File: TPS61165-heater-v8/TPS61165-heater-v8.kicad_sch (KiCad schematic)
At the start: 33 parts, among them J1 USB_C_KoreanHroparts_6P, J2 A2001WR-2P, J3 A2001WR-2P, J5 A2001WR-2P, U1 TPS61165, U2 KAQY212A, U3 INA219AxD

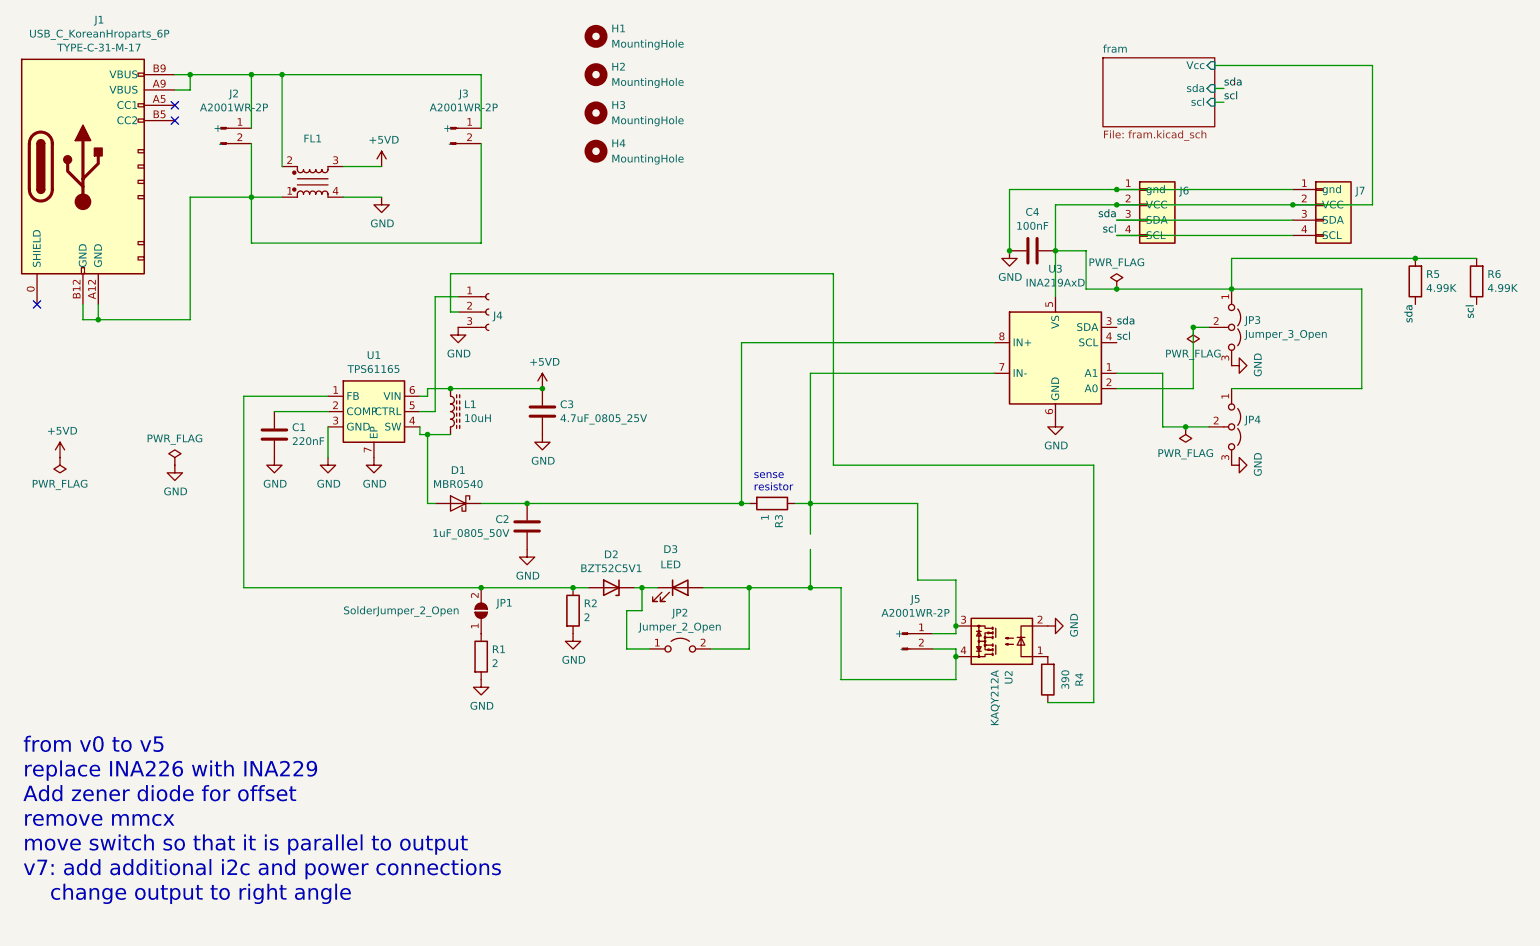
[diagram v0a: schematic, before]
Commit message: commit updates to high power heater
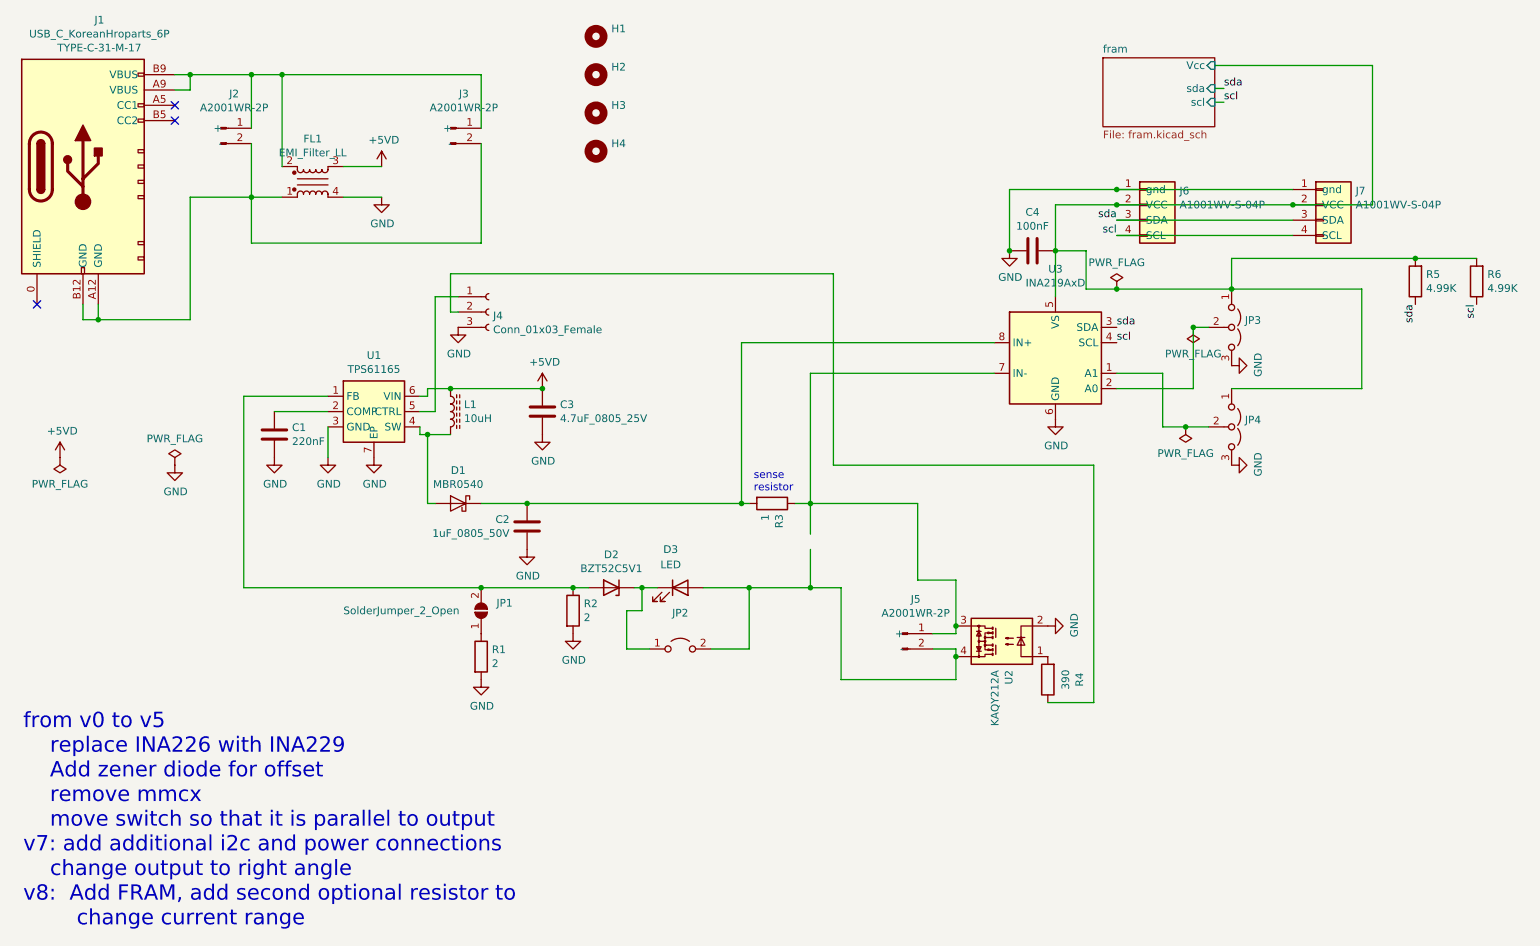
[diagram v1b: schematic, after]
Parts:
- FL1: value (none) -> EMI_Filter_LL; footprint (none) -> 0my_footprints6:LL_FILTER-SMD_4P-L9.2-W6.0-TL
- H1, H2, H3, H4: value MountingHole -> (none); footprint MountingHole:MountingHole_3.2mm_M3_Pad_TopBottom -> (none); now left out of the parts list
- J4: value (none) -> Conn_01x03_Female; footprint (none) -> Connector_PinSocket_2.54mm:PinSocket_1x03_P2.54mm_Horizontal
- J6, J7: value (none) -> A1001WV-S-04P; footprint (none) -> Connector_JST:JST_SH_BM04B-SRSS-TB_1x04-1MP_P1.00mm_Vertical
- JP2: value Jumper_2_Open -> (none); footprint Jumper:SolderJumper-2_P1.3mm_Open_RoundedPad1.0x1.5mm -> (none); now left out of the parts list
- JP3: value Jumper_3_Open -> (none); footprint Jumper:SolderJumper-3_P1.3mm_Open_Pad1.0x1.5mm -> (none); now left out of the parts list
- JP4: now left out of the parts list
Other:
- note added: "from v0 to v5 replace INA226 with INA229 Add zener diode for offset remove mmcx move switch so that it is parallel to output v7: add additional i2c and power connections change output to right angle v8: Add FRAM, add second optional resistor to change current range"
- note removed: "from v0 to v5 replace INA226 with INA229 Add zener diode for offset remove mmcx move switch so that it is parallel to output v7: add additional i2c and power connections change output to right angle"
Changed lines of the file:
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@@
     (stroke (width 0) (type default) (color 0 0 0 0))
   )
-  (text "from v0 to v5\nreplace INA226 with INA229\nAdd zener diode for offset\nremove mmcx\nmove switch so that it is parallel to output\nv7: add additional i2c and power connections\n    change output to right angle\n\n"
+  (text "from v0 to v5\n	replace INA226 with INA229\n	Add zener diode for offset\n	remove mmcx\n	move switch so that it is parallel to output\nv7: add additional i2c and power connections\n    change output to right angle\nv8:  Add FRAM, add second optional resistor to \n		change current range \n"
     (at 34.544 174.498 0)
     (effects (font (size 2.54 2.54)) (justify left bottom))
@@
     (in_bom yes) (on_board yes)
     (property "Reference" "FL1" (id 0) (at 82.55 43.6626 0))
-    (property "Value" "" (id 1) (at 82.55 45.974 0))
-    (property "Footprint" "" (id 2) (at 82.55 49.784 90)
+    (property "Value" "EMI_Filter_LL" (id 1) (at 82.55 45.974 0))
+    (property "Footprint" "0my_footprints6:LL_FILTER-SMD_4P-L9.2-W6.0-TL" (id 2) (at 82.55 49.784 90)
       (effects (font (size 1.27 1.27)) hide)
     )
@@
       (effects (font (size 1.27 1.27)) (justify left))
     )
-    (property "Value" "" (id 1) (at 112.4712 75.311 0)
-      (effects (font (size 1.27 1.27)) (justify left))
-    )
-    (property "Footprint" "" (id 2) (at 111.76 72.39 0)
+    (property "Value" "Conn_01x03_Female" (id 1) (at 112.4712 75.311 0)
+      (effects (font (size 1.27 1.27)) (justify left))
+    )
+    (property "Footprint" "Connector_PinSocket_2.54mm:PinSocket_1x03_P2.54mm_Horizontal" (id 2) (at 111.76 72.39 0)
       (effects (font (size 1.27 1.27)) hide)
     )
@@
       (effects (font (size 1.27 1.27)) (justify left))
     )
-    (property "Value" "" (id 1) (at 226.314 54.61 0)
-      (effects (font (size 1.27 1.27)) (justify left))
-    )
-    (property "Footprint" "" (id 2) (at 220.98 54.61 0)
+    (property "Value" "A1001WV-S-04P" (id 1) (at 226.314 54.61 0)
+      (effects (font (size 1.27 1.27)) (justify left))
+    )
+    (property "Footprint" "Connector_JST:JST_SH_BM04B-SRSS-TB_1x04-1MP_P1.00mm_Vertical" (id 2) (at 220.98 54.61 0)
       (effects (font (size 1.27 1.27)) hide)
     )
@@
   )
   (symbol (lib_id "Jumper:Jumper_3_Open") (at 234.95 74.93 270) (unit 1)
-    (in_bom yes) (on_board yes)
+    (in_bom no) (on_board yes)
     (property "Reference" "JP3" (id 0) (at 237.1598 73.7616 90)
       (effects (font (size 1.27 1.27)) (justify left))
     )
-    (property "Value" "Jumper_3_Open" (id 1) (at 237.1598 76.073 90)
-      (effects (font (size 1.27 1.27)) (justify left))
-    )
-    (property "Footprint" "Jumper:SolderJumper-3_P1.3mm_Open_Pad1.0x1.5mm" (id 2) (at 234.95 74.93 0)
+    (property "Value" "" (id 1) (at 237.1598 76.073 90)
+      (effects (font (size 1.27 1.27)) (justify left))
+    )
+    (property "Footprint" "" (id 2) (at 234.95 74.93 0)
       (effects (font (size 1.27 1.27)) hide)
     )
@@
   )
   (symbol (lib_id "Jumper:Jumper_3_Open") (at 234.95 91.44 270) (unit 1)
-    (in_bom yes) (on_board yes)
+    (in_bom no) (on_board yes)
     (property "Reference" "JP4" (id 0) (at 237.1598 90.2716 90)
       (effects (font (size 1.27 1.27)) (justify left))
@@
   )
   (symbol (lib_id "Jumper:Jumper_2_Open") (at 143.51 128.27 0) (unit 1)
-    (in_bom yes) (on_board yes)
+    (in_bom no) (on_board yes)
     (property "Reference" "JP2" (id 0) (at 143.51 122.301 0))
-    (property "Value" "Jumper_2_Open" (id 1) (at 143.51 124.6124 0))
-    (property "Footprint" "Jumper:SolderJumper-2_P1.3mm_Open_RoundedPad1.0x1.5mm" (id 2) (at 143.51 128.27 0)
+    (property "Value" "" (id 1) (at 143.51 124.6124 0))
+    (property "Footprint" "" (id 2) (at 143.51 128.27 0)
       (effects (font (size 1.27 1.27)) hide)
     )
@@
   )
   (symbol (lib_id "Mechanical:MountingHole") (at 129.54 45.72 0) (unit 1)
-    (in_bom yes) (on_board yes) (fields_autoplaced)
+    (in_bom no) (on_board yes) (fields_autoplaced)
     (property "Reference" "H4" (id 0) (at 132.08 44.4499 0)
       (effects (font (size 1.27 1.27)) (justify left))
     )
-    (property "Value" "MountingHole" (id 1) (at 132.08 46.9899 0)
-      (effects (font (size 1.27 1.27)) (justify left))
-    )
-    (property "Footprint" "MountingHole:MountingHole_3.2mm_M3_Pad_TopBottom" (id 2) (at 129.54 45.72 0)
+    (property "Value" "" (id 1) (at 132.08 46.9899 0)
+      (effects (font (size 1.27 1.27)) (justify left))
+    )
+    (property "Footprint" "" (id 2) (at 129.54 45.72 0)
       (effects (font (size 1.27 1.27)) hide)
     )
@@
   )
   (symbol (lib_id "Mechanical:MountingHole") (at 129.54 26.67 0) (unit 1)
-    (in_bom yes) (on_board yes) (fields_autoplaced)
+    (in_bom no) (on_board yes) (fields_autoplaced)
     (property "Reference" "H1" (id 0) (at 132.08 25.3999 0)
       (effects (font (size 1.27 1.27)) (justify left))
     )
-    (property "Value" "MountingHole" (id 1) (at 132.08 27.9399 0)
-      (effects (font (size 1.27 1.27)) (justify left))
-    )
-    (property "Footprint" "MountingHole:MountingHole_3.2mm_M3_Pad_TopBottom" (id 2) (at 129.54 26.67 0)
+    (property "Value" "" (id 1) (at 132.08 27.9399 0)
+      (effects (font (size 1.27 1.27)) (justify left))
+    )
+    (property "Footprint" "" (id 2) (at 129.54 26.67 0)
       (effects (font (size 1.27 1.27)) hide)
     )
@@
   )
   (symbol (lib_id "Mechanical:MountingHole") (at 129.54 33.02 0) (unit 1)
-    (in_bom yes) (on_board yes) (fields_autoplaced)
+    (in_bom no) (on_board yes) (fields_autoplaced)
     (property "Reference" "H2" (id 0) (at 132.08 31.7499 0)
       (effects (font (size 1.27 1.27)) (justify left))
     )
-    (property "Value" "MountingHole" (id 1) (at 132.08 34.2899 0)
-      (effects (font (size 1.27 1.27)) (justify left))
-    )
-    (property "Footprint" "MountingHole:MountingHole_3.2mm_M3_Pad_TopBottom" (id 2) (at 129.54 33.02 0)
+    (property "Value" "" (id 1) (at 132.08 34.2899 0)
+      (effects (font (size 1.27 1.27)) (justify left))
+    )
+    (property "Footprint" "" (id 2) (at 129.54 33.02 0)
       (effects (font (size 1.27 1.27)) hide)
     )
@@
   )
   (symbol (lib_id "Mechanical:MountingHole") (at 129.54 39.37 0) (unit 1)
-    (in_bom yes) (on_board yes) (fields_autoplaced)
+    (in_bom no) (on_board yes) (fields_autoplaced)
     (property "Reference" "H3" (id 0) (at 132.08 38.0999 0)
       (effects (font (size 1.27 1.27)) (justify left))
     )
-    (property "Value" "MountingHole" (id 1) (at 132.08 40.6399 0)
-      (effects (font (size 1.27 1.27)) (justify left))
-    )
-    (property "Footprint" "MountingHole:MountingHole_3.2mm_M3_Pad_TopBottom" (id 2) (at 129.54 39.37 0)
+    (property "Value" "" (id 1) (at 132.08 40.6399 0)
+      (effects (font (size 1.27 1.27)) (justify left))
+    )
+    (property "Footprint" "" (id 2) (at 129.54 39.37 0)
       (effects (font (size 1.27 1.27)) hide)
     )
@@
       (effects (font (size 1.27 1.27)) (justify left))
     )
-    (property "Value" "" (id 1) (at 255.524 54.61 0)
-      (effects (font (size 1.27 1.27)) (justify left))
-    )
-    (property "Footprint" "" (id 2) (at 250.19 54.61 0)
-      (effects (font (size 1.27 1.27)) hide)
-    )
+    (property "Value" "A1001WV-S-04P" (id 1) (at 255.524 54.61 0)
+      (effects (font (size 1.27 1.27)) (justify left))
+    )
+    (property "Footprint" "Connector_JST:JST_SH_BM04B-SRSS-TB_1x04-1MP_P1.00mm_Vertical" (id 2) (at 250.19 54.61 0)
+      (effects (font (size 1.27 1.27)) hide)
+    )
